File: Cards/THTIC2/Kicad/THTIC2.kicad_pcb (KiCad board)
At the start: 2 copper layers, 41.5 x 30.5 mm, 27 parts, among them J1 Conn_01x04_Pin, J2 Plasma 200V, U1 B0509S-1WR3, U2 ISO1540, U3 ADS1014IDGS, U4 LMV321, U5 AMS1117-5

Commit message: Gerbers done again.
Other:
- board text added: "MetalMusings THTIC2 March 2025"
- board text removed: "MetalMusings THTIC March 2025"
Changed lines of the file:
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@@
 		(layer "Edge.Cuts")
 	)
-	(gr_text "MetalMusings THTIC\nMarch 2025"
+	(gr_text "MetalMusings THTIC2\nMarch 2025"
 		(at 180.848 95.377 0)
 		(layer "B.SilkS")

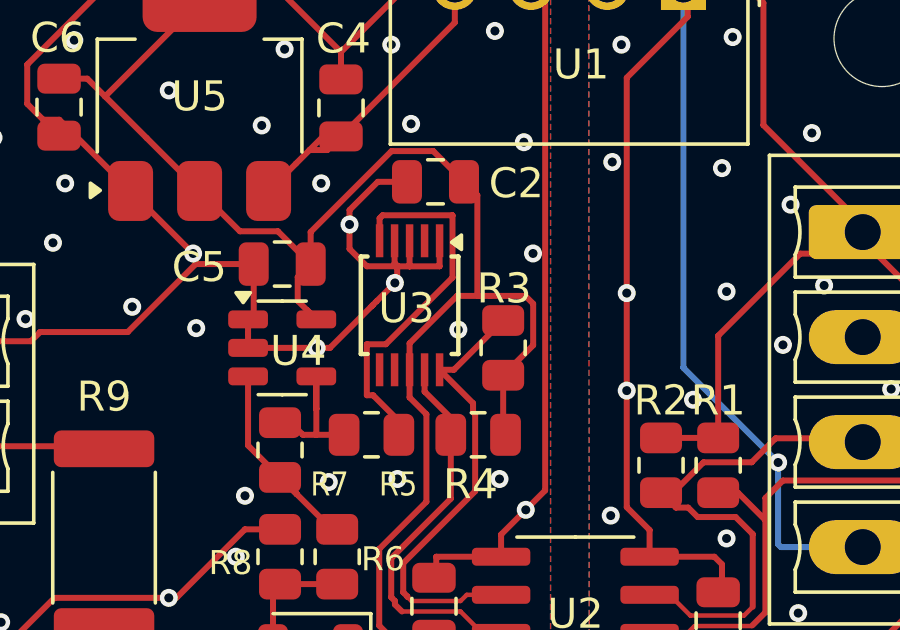
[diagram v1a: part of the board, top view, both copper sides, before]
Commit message: Shifted pin 0 and pin 1 for positive voltage value.
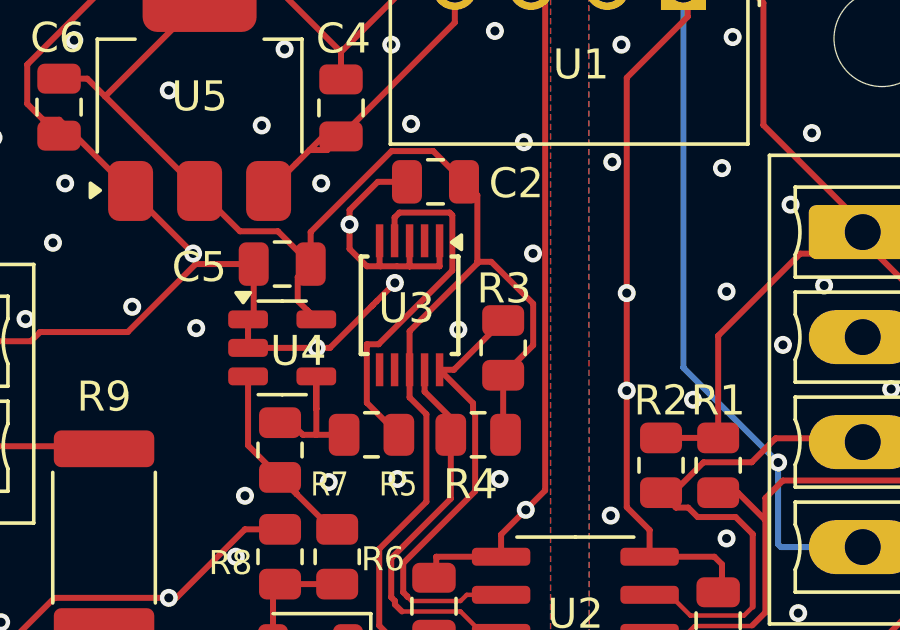
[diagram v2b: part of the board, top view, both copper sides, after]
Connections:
- R5 pad 1: Net-(U3-AIN1) -> Net-(U3-AIN0)
- U3 pad 4: GND_ISO -> Net-(U3-AIN0)
- U3 pad 5: Net-(U3-AIN1) -> GND_ISO
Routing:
- net Net-(U3-AIN1): track 12.7 -> 0.00 mm
- net Net-(U3-AIN0): track 0.00 -> 12.0 mm
- net GND_ISO: track 132.4 -> 131.9 mm
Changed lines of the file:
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@@
 	(net 12 "Net-(U4--)")
 	(net 13 "Net-(D1-A)")
-	(net 14 "Net-(U3-AIN1)")
+	(net 14 "Net-(U3-AIN0)")
 	(net 15 "unconnected-(U3-Pad6)")
 	(net 16 "unconnected-(U3-ALERT{slash}RDY-Pad2)")
@@
 			(layers "F.Cu" "F.Paste" "F.Mask")
 			(roundrect_rratio 0.243902)
-			(net 14 "Net-(U3-AIN1)")
+			(net 14 "Net-(U3-AIN0)")
 			(pintype "passive")
 		)
@@
 			(size 1.1 0.25)
 			(layers "F.Cu" "F.Paste" "F.Mask")
-			(net 3 "GND_ISO")
+			(net 14 "Net-(U3-AIN0)")
 			(pinfunction "AIN0")
 			(pintype "input")
@@
 			(size 1.1 0.25)
 			(layers "F.Cu" "F.Paste" "F.Mask")
-			(net 14 "Net-(U3-AIN1)")
+			(net 3 "GND_ISO")
 			(pinfunction "AIN1")
 			(pintype "input")
@@
 	)
 	(segment
+		(start 175.3108 95.22)
+		(end 174.851 95.22)
+		(width 0.2)
+		(layer "F.Cu")
+		(net 3)
+	)
+	(segment
 		(start 176.276 95.2217)
 		(end 176.276 95.2202)
@@
 	)
 	(segment
+		(start 175.276 94.37)
+		(end 175.276 95.1852)
+		(width 0.2)
+		(layer "F.Cu")
+		(net 3)
+	)
+	(segment
 		(start 163.653 97.719)
 		(end 163.96 97.4121)
@@
 	)
 	(segment
-		(start 175.7862 95.7762)
-		(end 175.1766 96.3858)
+		(start 175.8433 95.22)
+		(end 175.3108 95.22)
 		(width 0.2)
 		(layer "F.Cu")
@@
 	)
 	(segment
-		(start 170.892 97.4655)
-		(end 170.892 97.466)
+		(start 175.7862 95.7762)
+		(end 175.1766 96.3858)
 		(width 0.2)
 		(layer "F.Cu")
@@
 	)
 	(segment
-		(start 175.863 95.6994)
-		(end 175.7862 95.7762)
+		(start 170.892 97.4655)
+		(end 170.892 97.466)
 		(width 0.2)
 		(layer "F.Cu")
@@
 	)
 	(segment
-		(start 175.776 94.37)
-		(end 175.776 95.1131)
+		(start 166.881 97.4121)
+		(end 169.147 95.1465)
 		(width 0.2)
 		(layer "F.Cu")
@@
 	)
 	(segment
-		(start 166.881 97.4121)
-		(end 169.147 95.1465)
+		(start 176.278 95.2217)
+		(end 176.276 95.2202)
 		(width 0.2)
 		(layer "F.Cu")
@@
 	)
 	(segment
-		(start 176.278 95.2217)
-		(end 176.276 95.2202)
+		(start 175.276 95.1852)
+		(end 175.3108 95.22)
 		(width 0.2)
 		(layer "F.Cu")
@@
 	)
 	(segment
-		(start 175.776 95.1131)
-		(end 175.863 95.2003)
-		(width 0.2)
-		(layer "F.Cu")
-		(net 3)
-	)
-	(segment
 		(start 166.927 85.1021)
 		(end 171.015 85.1021)
@@
 	)
 	(segment
-		(start 175.863 95.2217)
-		(end 175.863 95.6994)
-		(width 0.2)
-		(layer "F.Cu")
-		(net 3)
-	)
-	(segment
 		(start 175.1766 96.3858)
 		(end 175.046 96.5164)
@@
 	)
 	(segment
-		(start 175.863 95.2003)
-		(end 175.8433 95.22)
-		(width 0.2)
-		(layer "F.Cu")
-		(net 3)
-	)
-	(segment
-		(start 175.8433 95.22)
-		(end 174.851 95.22)
-		(width 0.2)
-		(layer "F.Cu")
-		(net 3)
-	)
-	(segment
 		(start 175.046 96.5164)
 		(end 175.0411 96.5213)
@@
 	)
 	(segment
-		(start 175.863 95.2003)
-		(end 175.863 95.2217)
-		(width 0.2)
-		(layer "F.Cu")
-		(net 3)
-	)
-	(segment
 		(start 162.5855 108.1277)
 		(end 162.5855 108.1785)
@@
 	)
 	(segment
+		(start 175.863 95.6994)
+		(end 175.7862 95.7762)
+		(width 0.2)
+		(layer "F.Cu")
+		(net 3)
+	)
+	(segment
 		(start 176.276 94.37)
 		(end 176.276 95.2202)
@@
 	)
 	(segment
-		(start 178.0896 92.4052)
-		(end 178.535178 92.850778)
-		(width 0.2)
-		(layer "F.Cu")
-		(net 5)
-	)
-	(segment
 		(start 177.0646 91.3802)
 		(end 178.0896 92.4052)
@@
 	)
 	(segment
-		(start 176.276 97.79)
-		(end 176.276 98.67)
+		(start 164.592 88.966)
+		(end 165.533 88.966)
 		(width 0.2)
 		(layer "F.Cu")
@@
 	)
 	(segment
-		(start 164.592 88.966)
-		(end 165.533 88.966)
+		(start 172.858 96.6802)
+		(end 173.168 96.9902)
 		(width 0.2)
 		(layer "F.Cu")
@@
 	)
 	(segment
-		(start 172.858 96.6802)
-		(end 173.168 96.9902)
+		(start 178.535178 95.124422)
+		(end 176.276 97.3836)
 		(width 0.2)
 		(layer "F.Cu")
@@
 	)
 	(segment
-		(start 178.535178 92.850778)
-		(end 178.535178 96.180678)
+		(start 175.264 104.644)
+		(end 176.837 103.071)
 		(width 0.2)
 		(layer "F.Cu")
@@
 	)
 	(segment
-		(start 175.264 104.644)
-		(end 176.837 103.071)
+		(start 178.998678 95.070778)
+		(end 180.396 96.4681)
+		(width 0.2)
+		(layer "F.Cu")
+		(net 5)
+	)
+	(segment
+		(start 180.396 96.4681)
+		(end 180.396 97.853)
 		(width 0.2)
 		(layer "F.Cu")
@@
 	)
 	(segment
-		(start 165.533 88.966)
-		(end 166.127 89.56)
-		(width 0.2)
-		(layer "F.Cu")
-		(net 5)
-	)
-	(segment
-		(start 180.396 97.853)
-		(end 180.396 96.4681)
+		(start 178.535178 95.070778)
+		(end 178.998678 95.070778)
 		(width 0.2)
 		(layer "F.Cu")
@@
 	)
 	(segment
-		(start 178.562 96.2075)
-		(end 177.858 96.2075)
+		(start 178.535178 95.070778)
+		(end 178.535178 95.124422)
 		(width 0.2)
 		(layer "F.Cu")
@@
 	)
 	(segment
-		(start 180.396 96.4681)
-		(end 180.135 96.2075)
+		(start 165.533 88.966)
+		(end 166.127 89.56)
 		(width 0.2)
 		(layer "F.Cu")
@@
 	)
 	(segment
-		(start 177.858 96.2075)
-		(end 176.276 97.79)
-		(width 0.2)
-		(layer "F.Cu")
-		(net 5)
-	)
-	(segment
 		(start 179.396 98.853)
 		(end 179.396 100.532)
@@
 	)
 	(segment
-		(start 180.135 96.2075)
-		(end 178.9684 96.2075)
+		(start 178.0896 92.4052)
+		(end 178.535178 92.850778)
 		(width 0.2)
 		(layer "F.Cu")
@@
 	)
 	(segment
-		(start 179.396 98.853)
-		(end 180.396 97.853)
+		(start 178.535178 92.850778)
+		(end 178.535178 95.070778)
 		(width 0.2)
 		(layer "F.Cu")
@@
 	)
 	(segment
-		(start 178.535178 96.180678)
-		(end 178.562 96.2075)
+		(start 180.396 97.853)
+		(end 179.396 98.853)
 		(width 0.2)
 		(layer "F.Cu")
@@
 	)
 	(segment
-		(start 166.127 89.56)
-		(end 169.277 86.41)
+		(start 176.276 97.3836)
+		(end 176.276 98.67)
 		(width 0.2)
 		(layer "F.Cu")
@@
 	)
 	(segment
-		(start 178.9684 96.2075)
-		(end 178.562 96.2075)
+		(start 166.127 89.56)
+		(end 169.277 86.41)
 		(width 0.2)
 		(layer "F.Cu")
@@
 	)
 	(segment
-		(start 177.708 95.596)
-		(end 175.484 97.82)
+		(start 177.701 95.362385)
+		(end 175.243385 97.82)
 		(width 0.2)
 		(layer "F.Cu")
@@
 	)
 	(segment
-		(start 175.276 93.62)
-		(end 175.376 93.52)
+		(start 175.776 93.595)
+		(end 175.9408 93.4302)
 		(width 0.2)
 		(layer "F.Cu")
@@
 	)
 	(segment
-		(start 175.484 97.82)
-		(end 174.851 97.82)
+		(start 175.9408 93.4302)
+		(end 177.6112 93.4302)
 		(width 0.2)
 		(layer "F.Cu")
@@
 	(segment
 		(start 174.851 97.82)
-		(end 174.851 99.52)
+		(end 174.851 99.7705)
 		(width 0.2)
 		(layer "F.Cu")
@@
 	)
 	(segment
-		(start 177.708 93.527)
+		(start 177.6112 93.4302)
 		(end 177.701 93.52)
 		(width 0.2)
@@
 	)
 	(segment
-		(start 177.708 95.596)
-		(end 177.708 93.527)
-		(width 0.2)
-		(layer "F.Cu")
-		(net 14)
-	)
-	(segment
-		(start 175.918 100.3784)
-		(end 175.918 100.838)
-		(width 0.2)
-		(layer "F.Cu")
-		(net 14)
-	)
-	(segment
-		(start 174.851 99.52)
-		(end 175.0596 99.52)
+		(start 175.243385 97.82)
+		(end 174.851 97.82)
 		(width 0.2)
 		(layer "F.Cu")
@@
 	)
 	(segment
-		(start 175.0596 99.52)
-		(end 175.918 100.3784)
+		(start 177.701 93.52)
+		(end 177.701 95.362385)
 		(width 0.2)
 		(layer "F.Cu")
@@
 	)
 	(segment
-		(start 175.276 94.37)
-		(end 175.276 93.62)
+		(start 174.851 99.7705)
+		(end 175.9185 100.838)
 		(width 0.2)
 		(layer "F.Cu")
@@
 	)
 	(segment
-		(start 177.701 93.52)
-		(end 175.376 93.52)
+		(start 175.776 94.37)
+		(end 175.776 93.595)
 		(width 0.2)
 		(layer "F.Cu")
